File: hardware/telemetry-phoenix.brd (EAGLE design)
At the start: 65 x 56 mm, 113 parts, among them IC10 TPS70933, IC11 VN5160S-E, IC2 TPS70933, IC3 BME280, IC4 STM32L052C8T6, IC5 TPS62160, IC6 HX1, IC7 LMP7702, IC8 ADXL345, IC9 VN5160S-E, J1 GPS1, J2 RASPBERRYPI-GPIO, J3 POWER, J4 GPS2, J5 DNP, J6 SMA_EDGE, J9 IO, Q1 SI4202DY, Y1 32768, Y2 8M

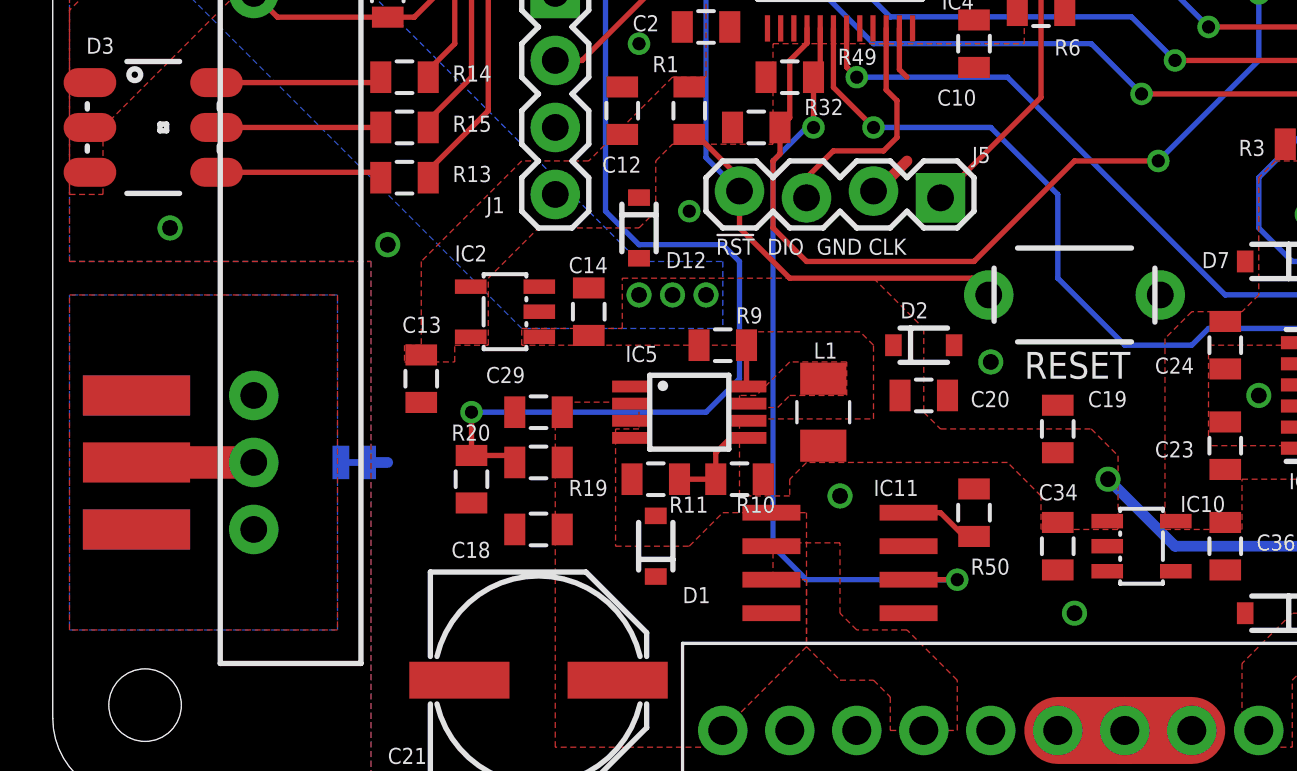
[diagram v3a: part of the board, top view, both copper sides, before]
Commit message: Adjust layout near regulator on Phoenix board
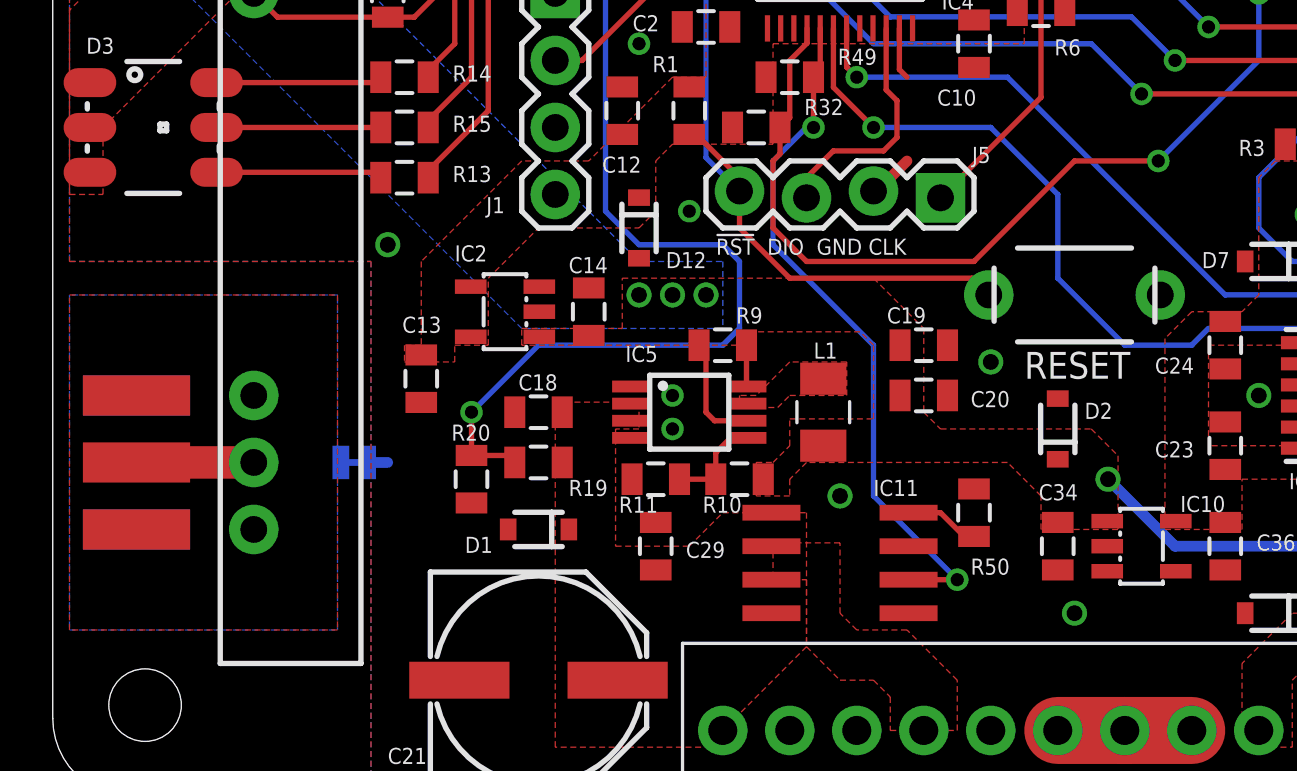
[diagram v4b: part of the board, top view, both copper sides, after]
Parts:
- moved C29 6.75 mm to (22.9, 9.53), turned to 90 degrees
- moved C19 5.99 mm to (33.0, 17.1), turned to 0 degrees
- moved D2 5.99 mm to (38.1, 14.0), turned to 90 degrees
- moved D1 4.49 mm to (18.4, 10.2), turned to 180 degrees
- moved C18 4.45 mm to (18.4, 14.6)
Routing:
- net 5V: track 26.3 -> 30.6 mm
- net K_RAD: track 29.9 -> 26.5 mm
- net VDIV: track 43.5 -> 42.4 mm
- net GND: vias 26 -> 27
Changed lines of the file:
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@@
 <attribute name="VALUE" x="52.832" y="18.034" size="0.6096" layer="27" ratio="15" rot="R90"/>
 </element>
-<element name="C18" library="SparkFun-Passives" package="0805" value="1u" x="18.415" y="10.16" smashed="yes" rot="R180">
-<attribute name="NAME" x="15.113" y="9.0805" size="0.6096" layer="25" ratio="15"/>
-<attribute name="VALUE" x="18.796" y="9.652" size="0.6096" layer="27" ratio="15" rot="R180"/>
-</element>
-<element name="C19" library="SparkFun-Passives" package="0805" value="10u" x="38.1" y="13.97" smashed="yes" rot="R90">
-<attribute name="NAME" x="39.243" y="14.7955" size="0.6096" layer="25" ratio="15"/>
-<attribute name="VALUE" x="39.497" y="12.954" size="0.6096" layer="27" ratio="15" rot="R90"/>
+<element name="C18" library="SparkFun-Passives" package="0805" value="1u" x="18.415" y="14.605" smashed="yes" rot="R180">
+<attribute name="NAME" x="17.653" y="15.4305" size="0.6096" layer="25" ratio="15"/>
+<attribute name="VALUE" x="18.796" y="14.097" size="0.6096" layer="27" ratio="15" rot="R180"/>
+</element>
+<element name="C19" library="SparkFun-Passives" package="0805" value="10u" x="33.02" y="17.145" smashed="yes">
+<attribute name="NAME" x="31.623" y="17.9705" size="0.6096" layer="25" ratio="15"/>
+<attribute name="VALUE" x="32.004" y="15.748" size="0.6096" layer="27" ratio="15"/>
 </element>
 <element name="C2" library="SparkFun-Passives" package="0805" value="0.1u" x="24.765" y="29.21" smashed="yes" rot="R180">
@@
 <attribute name="VALUE" x="6.604" y="47.498" size="0.6096" layer="27" ratio="15"/>
 </element>
-<element name="C29" library="SparkFun-Passives" package="0805" value="0.1u" x="18.415" y="14.605" smashed="yes" rot="R180">
-<attribute name="NAME" x="17.907" y="16.3195" size="0.6096" layer="25" ratio="15" rot="R180"/>
-<attribute name="VALUE" x="20.066" y="16.002" size="0.6096" layer="27" ratio="15" rot="R180"/>
+<element name="C29" library="SparkFun-Passives" package="0805" value="0.1u" x="22.86" y="9.525" smashed="yes" rot="R90">
+<attribute name="NAME" x="24.003" y="9.0805" size="0.6096" layer="25" ratio="15"/>
+<attribute name="VALUE" x="21.717" y="8.509" size="0.6096" layer="27" ratio="15" rot="R90"/>
 </element>
 <element name="C3" library="SparkFun-Passives" package="0805" value="0.1u" x="24.13" y="38.1" smashed="yes" rot="R180">
@@
 <attribute name="VALUE" x="37.719" y="43.688" size="0.6096" layer="27" ratio="15"/>
 </element>
-<element name="D1" library="SparkFun-DiscreteSemi" package="SOD-323" value="15V" x="22.86" y="9.525" smashed="yes" rot="R90">
-<attribute name="PROD_ID" value="DIO-12442" x="22.86" y="9.525" size="1.778" layer="27" rot="R90" display="off"/>
-<attribute name="NAME" x="23.876" y="7.366" size="0.6096" layer="25" ratio="15"/>
+<element name="D1" library="SparkFun-DiscreteSemi" package="SOD-323" value="15V" x="18.415" y="10.16" smashed="yes" rot="R180">
+<attribute name="PROD_ID" value="DIO-12442" x="18.415" y="10.16" size="1.778" layer="27" rot="R180" display="off"/>
+<attribute name="NAME" x="15.621" y="9.271" size="0.6096" layer="25" ratio="15"/>
 </element>
 <element name="D10" library="SparkFun-DiscreteSemi" package="SOD-323" value="5.6V" x="57.15" y="33.655" smashed="yes" rot="R90">
@@
 <attribute name="VALUE" x="47.371" y="8.382" size="0.6096" layer="27" ratio="15" rot="R180"/>
 </element>
-<element name="D2" library="SparkFun-DiscreteSemi" package="SOD-323" value="5.6V" x="33.02" y="17.145" smashed="yes">
-<attribute name="PROD_ID" value="DIO-12442" x="33.02" y="17.145" size="1.778" layer="27" display="off"/>
-<attribute name="NAME" x="32.131" y="18.161" size="0.6096" layer="25" ratio="15"/>
+<element name="D2" library="SparkFun-DiscreteSemi" package="SOD-323" value="5.6V" x="38.1" y="13.97" smashed="yes" rot="R90">
+<attribute name="PROD_ID" value="DIO-12442" x="38.1" y="13.97" size="1.778" layer="27" rot="R90" display="off"/>
+<attribute name="NAME" x="39.116" y="14.351" size="0.6096" layer="25" ratio="15"/>
 </element>
 <element name="D3" library="SparkFun-LED" package="LED-TRICOLOR-5050" value="COM-10866" x="3.81" y="25.4" smashed="yes">
@@
 <element name="IC5" library="HAB" package="MSOP8" value="TPS62160" x="24.13" y="14.605" smashed="yes" rot="R270">
 <attribute name="NAME" x="21.71" y="16.51" size="0.6096" layer="25" ratio="15"/>
-<attribute name="VALUE" x="23.114" y="17.795" size="0.6096" layer="27" ratio="15" rot="R270"/>
+<attribute name="VALUE" x="23.48" y="16.129" size="0.6096" layer="27" ratio="15"/>
 </element>
 <element name="IC6" library="HAB" package="HX1" value="HX1" x="7.62" y="10.16" smashed="yes" rot="R90">
@@
 </element>
 <element name="R10" library="SparkFun-Passives" package="0805" value="430K" x="26.035" y="12.065" smashed="yes">
-<attribute name="NAME" x="25.908" y="10.795" size="0.6096" layer="25" ratio="15"/>
+<attribute name="NAME" x="24.638" y="10.795" size="0.6096" layer="25" ratio="15"/>
 <attribute name="VALUE" x="25.019" y="12.573" size="0.6096" layer="27" ratio="15"/>
 </element>
 <element name="R11" library="SparkFun-Passives" package="0805" value="82K" x="22.86" y="12.065" smashed="yes">
-<attribute name="NAME" x="23.368" y="10.795" size="0.6096" layer="25" ratio="15"/>
+<attribute name="NAME" x="21.463" y="10.795" size="0.6096" layer="25" ratio="15"/>
 <attribute name="VALUE" x="22.479" y="12.573" size="0.6096" layer="27" ratio="15"/>
 </element>
@@
 <wire x1="29.095" y1="38.155" x2="29.095" y2="39.255" width="0.2032" layer="1"/>
 <wire x1="29.095" y1="39.255" x2="29.21" y2="39.37" width="0.2032" layer="1"/>
-<via x="4.445" y="21.59" extent="1-16" drill="0.6"/>
 <via x="12.7" y="20.955" extent="1-16" drill="0.6"/>
 <via x="23.495" y="36.83" extent="1-16" drill="0.5"/>
@@
 <via x="50.165" y="34.671" extent="1-16" drill="0.5"/>
 <via x="59.69" y="25.4" extent="1-16" drill="0.5"/>
+<via x="23.495" y="15.24" extent="1-16" drill="0.5"/>
+<via x="23.495" y="13.97" extent="1-16" drill="0.5"/>
 </signal>
 <signal name="VDDA">
@@
 <contactref element="C28" pad="1"/>
 <polygon width="0.2032" layer="1" isolate="0.2032" rank="2">
-<vertex x="26.035" y="14.351"/>
+<vertex x="27.94" y="14.351"/>
 <vertex x="31.115" y="14.351"/>
 <vertex x="31.115" y="17.145"/>
@@
 <vertex x="27.94" y="12.065"/>
 <vertex x="27.94" y="11.43"/>
-<vertex x="26.035" y="11.43"/>
+<vertex x="26.67" y="11.43"/>
+<vertex x="26.67" y="12.7"/>
+<vertex x="27.305" y="12.7"/>
+<vertex x="27.94" y="13.335"/>
 </polygon>
 <polygon width="0.2032" layer="1" isolate="0.3048" rank="3">
@@
 <wire x1="60.325" y1="13.065" x2="58.785" y2="13.065" width="0.4064" layer="1"/>
 <wire x1="58.785" y1="13.065" x2="58.42" y2="12.7" width="0.4064" layer="1"/>
+<wire x1="26.33" y1="14.28" x2="25.09" y2="14.28" width="0.2032" layer="1"/>
+<wire x1="25.09" y1="14.28" x2="24.765" y2="14.605" width="0.2032" layer="1"/>
+<wire x1="24.765" y1="14.605" x2="24.765" y2="16.88" width="0.2032" layer="1"/>
+<wire x1="24.765" y1="16.88" x2="24.5" y2="17.145" width="0.2032" layer="1"/>
 </signal>
 <signal name="SCL">
@@
 <wire x1="22.225" y1="20.955" x2="25.4" y2="20.955" width="0.2032" layer="16"/>
 <wire x1="25.4" y1="20.955" x2="26.035" y2="20.32" width="0.2032" layer="16"/>
-<wire x1="26.035" y1="20.32" x2="26.035" y2="15.875" width="0.2032" layer="16"/>
-<wire x1="26.035" y1="15.875" x2="24.765" y2="14.605" width="0.2032" layer="16"/>
-<wire x1="24.765" y1="14.605" x2="15.875" y2="14.605" width="0.2032" layer="16"/>
+<wire x1="26.035" y1="20.32" x2="26.035" y2="17.78" width="0.2032" layer="16"/>
+<wire x1="26.035" y1="17.78" x2="25.4" y2="17.145" width="0.2032" layer="16"/>
+<wire x1="25.4" y1="17.145" x2="18.415" y2="17.145" width="0.2032" layer="16"/>
+<wire x1="18.415" y1="17.145" x2="15.875" y2="14.605" width="0.2032" layer="16"/>
 <via x="15.875" y="14.605" extent="1-16" drill="0.5"/>
 <wire x1="15.875" y1="14.605" x2="15.875" y2="12.965" width="0.2032" layer="1"/>
@@
 <wire x1="28.84" y1="25.4" x2="28.575" y2="25.4" width="0.2032" layer="16"/>
 <wire x1="28.575" y1="25.4" x2="27.305" y2="24.13" width="0.2032" layer="16"/>
-<wire x1="27.305" y1="24.13" x2="27.305" y2="9.525" width="0.2032" layer="16"/>
-<wire x1="27.305" y1="9.525" x2="28.575" y2="8.255" width="0.2032" layer="16"/>
-<wire x1="28.575" y1="8.255" x2="34.29" y2="8.255" width="0.2032" layer="16"/>
+<wire x1="27.305" y1="24.13" x2="27.305" y2="20.955" width="0.2032" layer="16"/>
+<wire x1="27.305" y1="20.955" x2="31.115" y2="17.145" width="0.2032" layer="16"/>
+<wire x1="31.115" y1="17.145" x2="31.115" y2="11.43" width="0.2032" layer="16"/>
+<wire x1="31.115" y1="11.43" x2="34.29" y2="8.255" width="0.2032" layer="16"/>
 <via x="34.29" y="8.255" extent="1-16" drill="0.5"/>
 <wire x1="34.29" y1="8.255" x2="32.445" y2="8.255" width="0.2032" layer="1"/>

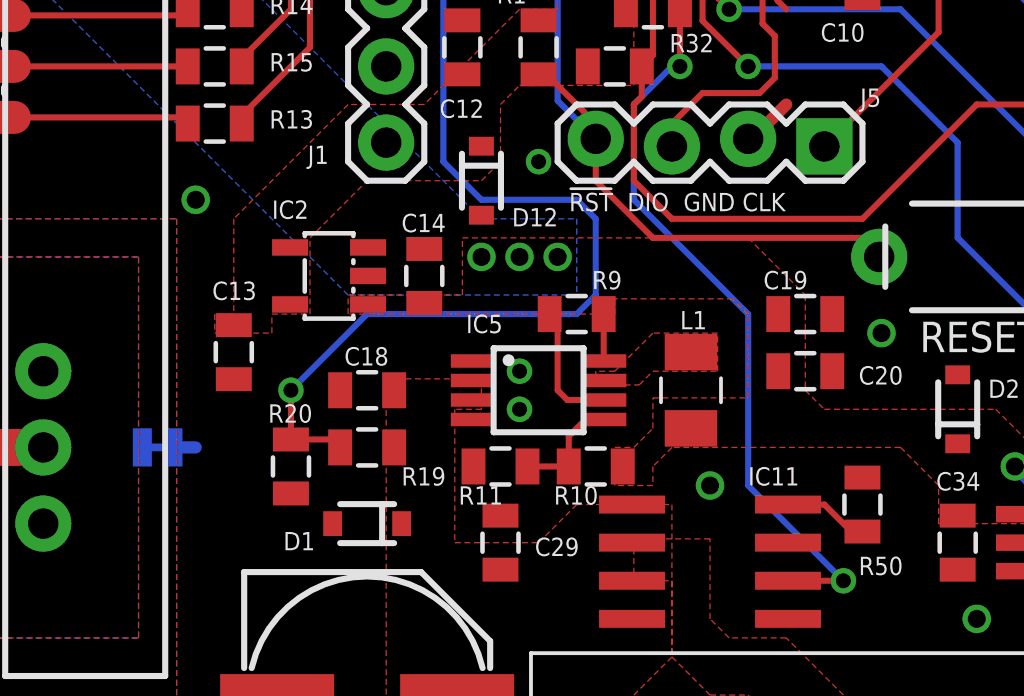
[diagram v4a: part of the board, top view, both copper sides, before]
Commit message: Satisfy Adi on Phoenix power supply routing
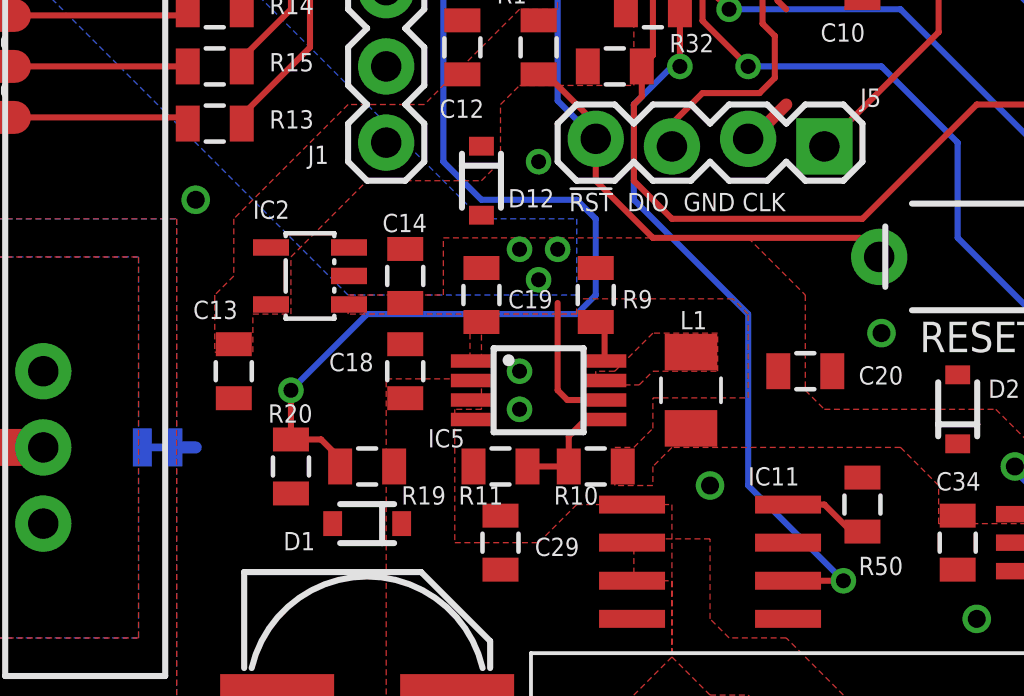
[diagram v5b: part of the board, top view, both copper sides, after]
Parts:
- moved C19 10.8 mm to (22.2, 17.8), turned to 270 degrees
- moved C18 1.42 mm to (19.7, 15.2), turned to 90 degrees
- moved R9 0.90 mm to (26.0, 17.8), turned to 90 degrees
- moved C14 0.64 mm to (19.7, 18.4)
- moved C13 0.63 mm to (14.0, 15.2)
- moved R19 0.63 mm to (18.4, 12.1)
- moved IC2 0.63 mm to (16.5, 18.4)

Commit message: A few minor tweaks to Phoenix board
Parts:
- moved R10 4.62 mm to (30.5, 13.3)
- moved L1 2.54 mm to (29.2, 17.1), turned to 180 degrees
- moved R11 2.54 mm to (25.4, 12.1)
- moved C29 1.27 mm to (22.9, 10.8)
- moved C20 0.63 mm to (33.0, 15.9)
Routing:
- net K_RAD: track 26.5 -> 28.4 mm
- net FB5: track 3.81 -> 5.50 mm
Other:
- board text added: "1"
